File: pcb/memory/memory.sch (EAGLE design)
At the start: 19 parts, among them IC1 XMEGA16, IC2 24LC512, U1 AS6C1008-55PCN

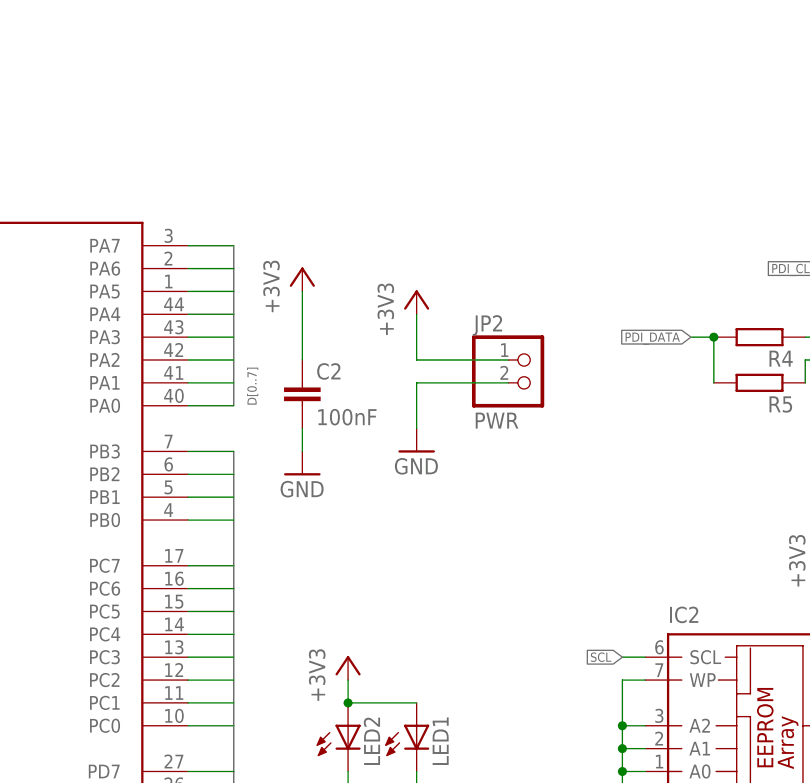
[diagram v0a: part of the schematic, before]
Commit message: Memory board schic: UART connectors
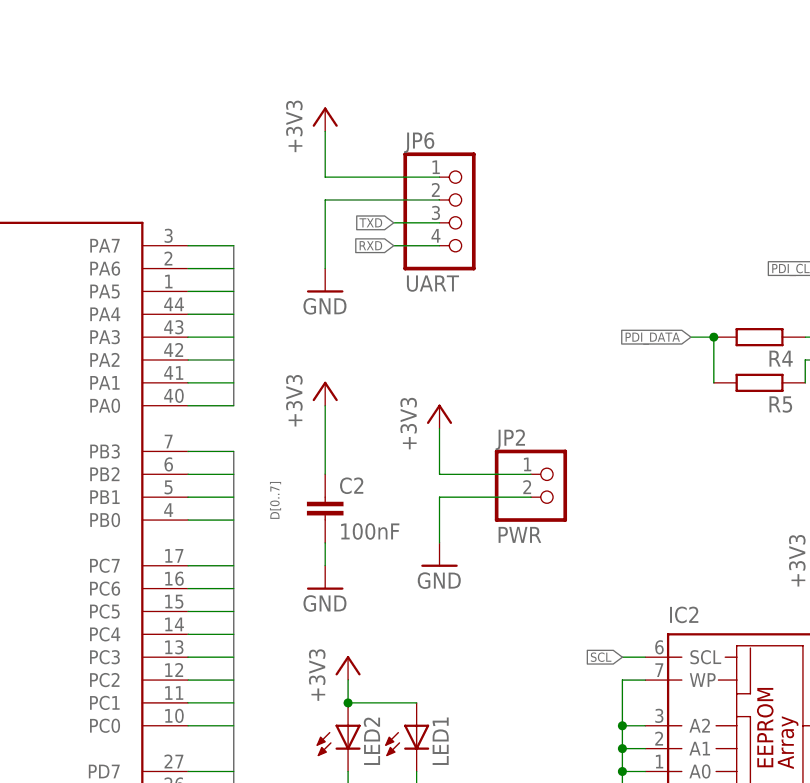
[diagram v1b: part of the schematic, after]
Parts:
- added JP6: UART, pinhead:PINHD-1X4
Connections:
- net +3V3: now also JP6.1
- net GND: now also JP6.2
- net RXD: now also JP6.4
- net TXD: now also JP6.3
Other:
- moved on the sheet: C2, JP2
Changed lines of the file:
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@@
 <part name="JP5" library="jumper" deviceset="JP1E" device=""/>
 <part name="+3V10" library="supply1" deviceset="+3V3" device=""/>
+<part name="JP6" library="pinhead" deviceset="PINHD-1X4" device="" value="UART"/>
+<part name="GND6" library="supply1" deviceset="GND" device=""/>
+<part name="+3V7" library="supply1" deviceset="+3V3" device=""/>
 </parts>
 <sheets>
@@
 </plain>
 <instances>
-<instance part="GND4" gate="1" x="132.08" y="86.36"/>
-<instance part="+3V2" gate="G$1" x="132.08" y="109.22"/>
-<instance part="C2" gate="G$1" x="132.08" y="96.52"/>
+<instance part="GND4" gate="1" x="134.62" y="73.66"/>
+<instance part="+3V2" gate="G$1" x="134.62" y="96.52"/>
+<instance part="C2" gate="G$1" x="134.62" y="83.82"/>
 <instance part="JP1" gate="A" x="236.22" y="93.98"/>
 <instance part="JP3" gate="A" x="236.22" y="50.8"/>
@@
 <instance part="R4" gate="G$1" x="182.88" y="101.6" rot="R180"/>
 <instance part="R5" gate="G$1" x="182.88" y="96.52" rot="R180"/>
-<instance part="JP2" gate="G$1" x="157.48" y="96.52"/>
-<instance part="+3V9" gate="G$1" x="144.78" y="106.68"/>
-<instance part="GND7" gate="1" x="144.78" y="88.9"/>
+<instance part="JP2" gate="G$1" x="160.02" y="83.82"/>
+<instance part="+3V9" gate="G$1" x="147.32" y="93.98"/>
+<instance part="GND7" gate="1" x="147.32" y="76.2"/>
 <instance part="R6" gate="G$1" x="144.78" y="45.72" rot="R90"/>
 <instance part="R7" gate="G$1" x="137.16" y="45.72" rot="R90"/>
@@
 <instance part="JP5" gate="A" x="63.5" y="129.54"/>
 <instance part="+3V10" gate="G$1" x="73.66" y="134.62"/>
+<instance part="JP6" gate="A" x="149.86" y="114.3"/>
+<instance part="GND6" gate="1" x="134.62" y="106.68"/>
+<instance part="+3V7" gate="G$1" x="134.62" y="127"/>
 </instances>
 <busses>
@@
 <segment>
 <wire x1="124.46" y1="111.76" x2="124.46" y2="93.98" width="0.762" layer="92"/>
-<label x="127" y="93.98" size="1.016" layer="95" rot="R90"/>
+<label x="129.54" y="81.28" size="1.016" layer="95" rot="R90"/>
 </segment>
 </bus>
@@
 <pinref part="C2" gate="G$1" pin="1"/>
 <pinref part="+3V2" gate="G$1" pin="+3V3"/>
-<wire x1="132.08" y1="99.06" x2="132.08" y2="106.68" width="0.1524" layer="91"/>
+<wire x1="134.62" y1="86.36" x2="134.62" y2="93.98" width="0.1524" layer="91"/>
 </segment>
 <segment>
@@
 <pinref part="JP2" gate="G$1" pin="1"/>
 <pinref part="+3V9" gate="G$1" pin="+3V3"/>
-<wire x1="154.94" y1="99.06" x2="144.78" y2="99.06" width="0.1524" layer="91"/>
-<wire x1="144.78" y1="99.06" x2="144.78" y2="104.14" width="0.1524" layer="91"/>
+<wire x1="157.48" y1="86.36" x2="147.32" y2="86.36" width="0.1524" layer="91"/>
+<wire x1="147.32" y1="86.36" x2="147.32" y2="91.44" width="0.1524" layer="91"/>
 </segment>
 <segment>
@@
 <wire x1="73.66" y1="127" x2="73.66" y2="132.08" width="0.1524" layer="91"/>
 </segment>
+<segment>
+<pinref part="JP6" gate="A" pin="1"/>
+<pinref part="+3V7" gate="G$1" pin="+3V3"/>
+<wire x1="147.32" y1="119.38" x2="134.62" y2="119.38" width="0.1524" layer="91"/>
+<wire x1="134.62" y1="119.38" x2="134.62" y2="124.46" width="0.1524" layer="91"/>
+</segment>
 </net>
 <net name="GND" class="0">
@@
 <pinref part="C2" gate="G$1" pin="2"/>
 <pinref part="GND4" gate="1" pin="GND"/>
-<wire x1="132.08" y1="91.44" x2="132.08" y2="88.9" width="0.1524" layer="91"/>
+<wire x1="134.62" y1="78.74" x2="134.62" y2="76.2" width="0.1524" layer="91"/>
 </segment>
 <segment>
@@
 <pinref part="JP2" gate="G$1" pin="2"/>
 <pinref part="GND7" gate="1" pin="GND"/>
-<wire x1="154.94" y1="96.52" x2="144.78" y2="96.52" width="0.1524" layer="91"/>
-<wire x1="144.78" y1="96.52" x2="144.78" y2="91.44" width="0.1524" layer="91"/>
+<wire x1="157.48" y1="83.82" x2="147.32" y2="83.82" width="0.1524" layer="91"/>
+<wire x1="147.32" y1="83.82" x2="147.32" y2="78.74" width="0.1524" layer="91"/>
+</segment>
+<segment>
+<pinref part="JP6" gate="A" pin="2"/>
+<pinref part="GND6" gate="1" pin="GND"/>
+<wire x1="147.32" y1="116.84" x2="134.62" y2="116.84" width="0.1524" layer="91"/>
+<wire x1="134.62" y1="116.84" x2="134.62" y2="109.22" width="0.1524" layer="91"/>
 </segment>
 </net>
@@
 <label x="124.46" y="43.18" size="1.016" layer="95" xref="yes"/>
 </segment>
+<segment>
+<pinref part="JP6" gate="A" pin="3"/>
+<wire x1="147.32" y1="114.3" x2="142.24" y2="114.3" width="0.1524" layer="91"/>
+<label x="142.24" y="114.3" size="1.016" layer="95" rot="R180" xref="yes"/>
+</segment>
 </net>
 <net name="RXD" class="0">
@@
 <label x="124.46" y="40.64" size="1.016" layer="95" xref="yes"/>
 </segment>
-</net>
+<segment>
+<pinref part="JP6" gate="A" pin="4"/>
+<wire x1="147.32" y1="111.76" x2="142.24" y2="111.76" width="0.1524" layer="91"/>
+<label x="142.24" y="111.76" size="1.016" layer="95" rot="R180" xref="yes"/>
+</segment>
+</net>
